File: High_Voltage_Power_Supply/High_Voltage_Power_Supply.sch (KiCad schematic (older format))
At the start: 36 parts

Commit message: Finalised the schematic and BOM
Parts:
- removed C?: 10uF, symbol Device:C
- removed D? (x5): D_ALT, symbol Device:D_ALT
- removed J?: Conn_01x01_Female, symbol Connector:Conn_01x01_Female
- removed R?: 100k, symbol Device:R
- removed R?: 2M, symbol Device:R
- removed R? (x3): 4m, symbol Device:R
- removed R?: 453k, symbol Device:R
- removed R?: inf, symbol Device:R
- added C3: 100uF, Capacitor_THT:CP_Radial_D8.0mm_P5.00mm, symbol Device:CP
- added C6: 10uF, Capacitor_SMD:C_1210_3225Metric, symbol Device:C
- added C8: 1000uF, Capacitor_THT:CP_Radial_D18.0mm_P7.50mm, symbol Device:CP
- added J4: Conn_01x02_Female, Connector_PinHeader_2.54mm:PinHeader_1x02_P2.54mm_Vertical, symbol Connector:Conn_01x02_Female
- added JP1: Jumper_2_Open, Resistor_SMD:R_0603_1608Metric, symbol Jumper:Jumper_2_Open
- added R10: 100k, Resistor_SMD:R_0603_1608Metric, symbol Device:R
- added R12: 453k, Resistor_SMD:R_0805_2012Metric, symbol Device:R
- added R16: 2M, Resistor_SMD:R_1206_3216Metric, symbol Device:R
- added R6, R7, R8: 4m, Resistor_SMD:R_2512_6332Metric, symbol Device:R
- C1: renamed from C?; footprint (none) -> Capacitor_SMD:C_1812_4532Metric; Link (none) -> https://www.digikey.com/product-detail/en/murata-electronic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; Voltage (none) -> >1200V
- C2: renamed from C?; footprint (none) -> Capacitor_SMD:C_0603_1608Metric; Link (none) -> https://www.digikey.com/product-detail/en/murata-electronic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
- C4: renamed from C?; footprint (none) -> Capacitor_SMD:C_1206_3216Metric; Link (none) -> https://www.digikey.com/product-detail/en/murata-electronic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
- C5: renamed from C?; footprint (none) -> Capacitor_SMD:C_1210_3225Metric; Link (none) -> https://www.digikey.com/product-detail/en/murata-electronic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
- C7: renamed from C?; footprint (none) -> Capacitor_THT:CP_Radial_D18.0mm_P7.50mm; Link (none) -> https://www.digikey.com/product-detail/en/nichicon/UPW2A102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
- D1: renamed from D?; value D_ALT -> NDSH25170A; footprint (none) -> Package_TO_SOT_THT:TO-247-2_Vertical; Link (none) -> https://www.digikey.com/product-detail/en/on-semiconductor/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
- J1, J2, J3: renamed from J?; footprint (none) -> Connector:Banana_Jack_2Pin
- Q1: renamed from Q?; footprint (none) -> Package_TO_SOT_THT:TO-264-3_Vertical; symbol Device:Q_NMOS_DGS -> Device:Q_NMOS_SDG; Link (none) -> https://www.digikey.com/product-detail/en/ixys/IXFK180N25T/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
- R1, R2, R3, R9: renamed from R?; footprint (none) -> Resistor_SMD:R_0603_1608Metric; Link (none) -> https://www.digikey.com/product-detail/en/panasonic-electro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
- R11, R13, R14: renamed from R?; footprint (none) -> Resistor_SMD:R_0805_2012Metric; Link (none) -> https://www.digikey.com/product-detail/en/panasonic-electro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; Search https://www.digikey.com/products/en/resistors/chip-resistor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 -> (none)
- R15: renamed from R?; footprint (none) -> Resistor_SMD:R_1206_3216Metric; Link (none) -> https://www.digikey.com/product-detail/en/panasonic-electro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; Search https://www.digikey.com/products/en/resistors/chip-resistor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 -> (none)
- R17: renamed from R?; footprint (none) -> Resistor_SMD:R_1206_3216Metric; Link (none) -> https://www.digikey.com/product-detail/en/panasonic-electro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; search https://www.digikey.com/products/en/resistors/chip-resistor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 -> (none)
- R4: renamed from R?; footprint (none) -> Resistor_SMD:R_0603_1608Metric; 681 Link (none) -> https://www.digikey.com/product-detail/en/panasonic-electro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; 681 search https://www.digikey.com/products/en/resistors/chip-resistor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 -> (none); 787 Link (none) -> https://www.digikey.com/product-detail/en/panasonic-electro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; 787 search https://www.digikey.com/products/en/resistors/chip-resistor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 -> (none)
- R5: renamed from R?; footprint (none) -> Resistor_SMD:R_2512_6332Metric; Link (none) -> https://www.digikey.com/product-detail/en/panasonic-electro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; Search https://www.digikey.com/products/en/resistors/chip-resistor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 -> (none)
- U1: renamed from U?; Link (LT3751E) (none) -> https://www.digikey.com/product-detail/en/analog-devices-in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
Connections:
- wire segments 102 -> 99
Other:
- moved on the sheet: J2

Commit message: Started on the PCB
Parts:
- J1: footprint Connector:Banana_Jack_2Pin -> Connector_PinHeader_2.54mm:PinHeader_1x02_P2.54mm_Vertical
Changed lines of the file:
@@
 F 0 "J1" H 4450 6050 50  0000 C CNN
 F 1 "Conn_01x02_Female" H 4700 5950 50  0000 C CNN
-F 2 "Connector:Banana_Jack_2Pin" H 4450 6250 50  0001 C CNN
+F 2 "Connector_PinHeader_2.54mm:PinHeader_1x02_P2.54mm_Vertical" H 4450 6250 50  0001 C CNN
 F 3 "~" H 4450 6250 50  0001 C CNN
 F 4 "12V" H 4450 6250 50  0001 C CNN "Voltage"
@@
 $EndComp
 $Comp
-L power:GND #PWR?
+L power:GND #PWR0118
 U 1 1 5F322467
 P 2900 3000
-F 0 "#PWR?" H 2900 2750 50  0001 C CNN
+F 0 "#PWR0118" H 2900 2750 50  0001 C CNN
 F 1 "GND" H 2905 2827 50  0000 C CNN
 F 2 "" H 2900 3000 50  0001 C CNN

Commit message: Finished most of the PCB layout
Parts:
- Q1: value Q_NMOS_DGS -> Q_NMOS_GDS; symbol Device:Q_NMOS_SDG -> Device:Q_NMOS_GDS
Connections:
- net at R5.1, R6.1, R7.1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: now also Q1.3 (S); no longer Q1.1 (S)
- net at U1.15 (HVGATE): now also Q1.1 (G); no longer Q1.3 (G)
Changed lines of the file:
@@
 $EndComp
 $Comp
-L Device:Q_NMOS_SDG Q1
+L Device:Q_NMOS_GDS Q1
 U 1 1 5B8B01E1
 P 5400 3400
 F 0 "Q1" H 5605 3446 50  0000 L CNN
-F 1 "Q_NMOS_DGS" H 5605 3355 50  0000 L CNN
+F 1 "Q_NMOS_GDS" H 5605 3355 50  0000 L CNN
 F 2 "Package_TO_SOT_THT:TO-264-3_Vertical" H 5600 3500 50  0001 C CNN
 F 3 "http://ixapps.ixys.com/DataSheet/DS100129A(IXFK-FX180N25T).pdf" H 5400 3400 50  0001 C CNN

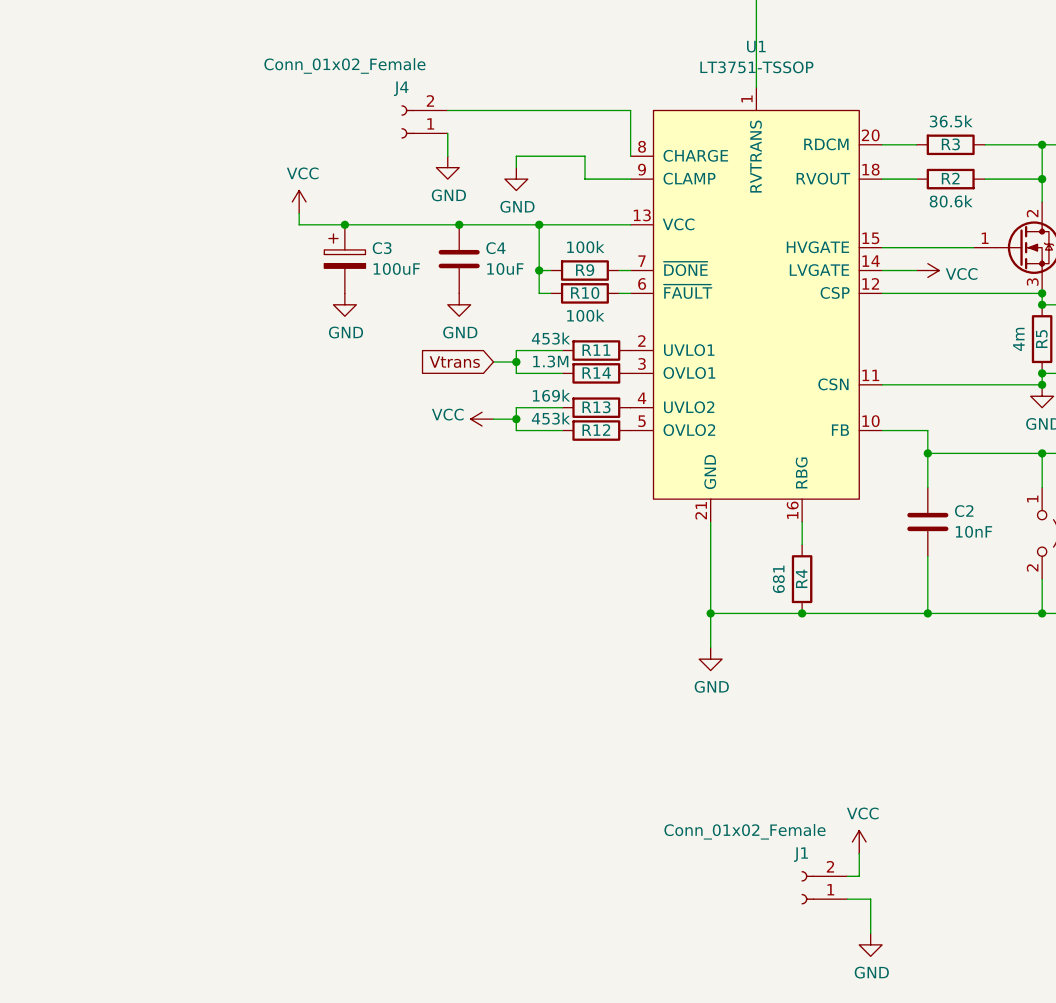
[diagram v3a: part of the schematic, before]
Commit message: Added Done and Fault outputs
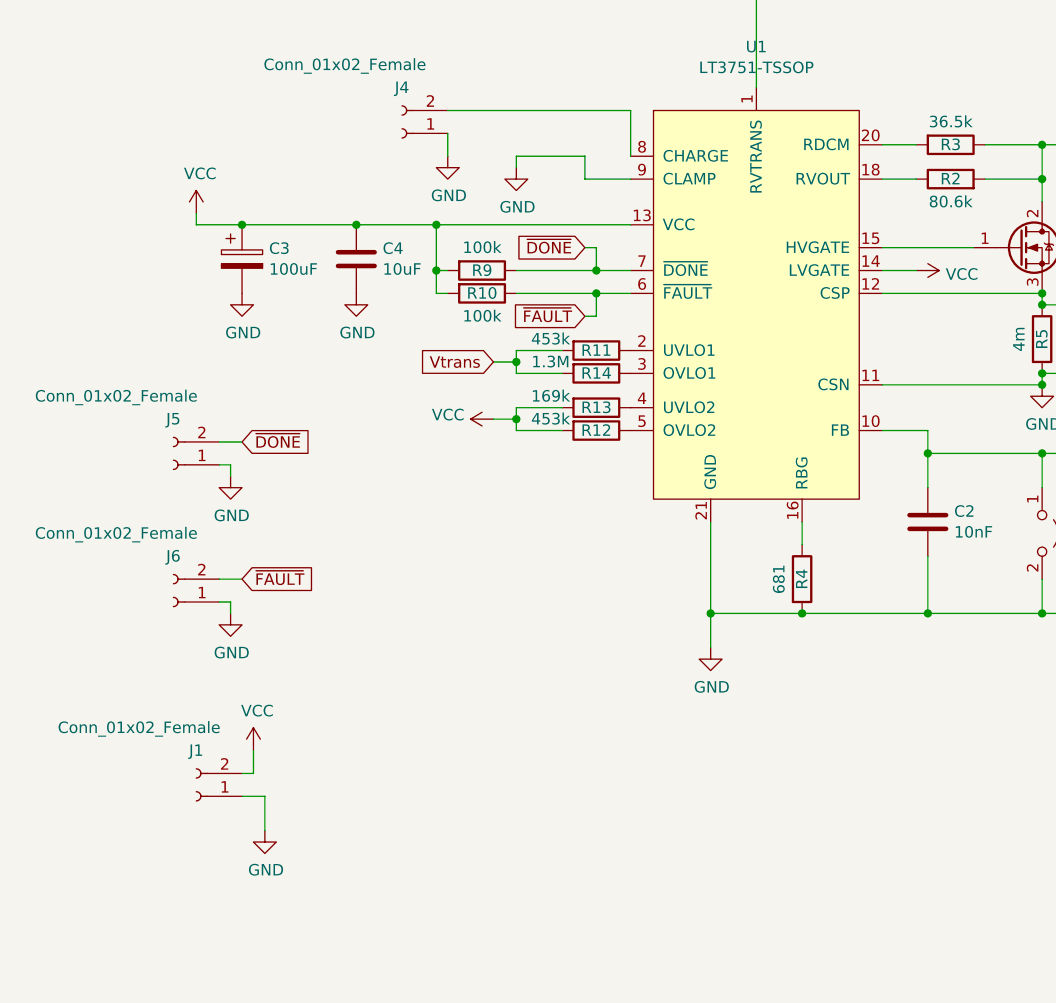
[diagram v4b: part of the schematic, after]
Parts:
- added J5, J6: Conn_01x02_Female, Connector_PinHeader_2.54mm:PinHeader_1x02_P2.54mm_Vertical, symbol Connector:Conn_01x02_Female
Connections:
- net GND: now also J5.1 (Pin_1), J6.1 (Pin_1)
- net ~FAULT~: now reaches R10.1, U1.6 (~FAULT~)
- net ~FAULT~: now also J6.2 (Pin_2)
- net ~DONE~: now reaches R9.1, U1.7 (~DONE~)
- net ~DONE~: now also J5.2 (Pin_2)
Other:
- moved on the sheet: C3, C4, J1, R10, R9

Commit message: Added some notes for it
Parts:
- J3: Voltage (none) -> 1000V
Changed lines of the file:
@@
 F 2 "Connector:Banana_Jack_2Pin" H 9800 2800 50  0001 C CNN
 F 3 "~" H 9800 2800 50  0001 C CNN
+F 4 "1000V" H 9800 2800 50  0001 C CNN "Voltage"
 	1    9800 2800
 	1    0    0    1

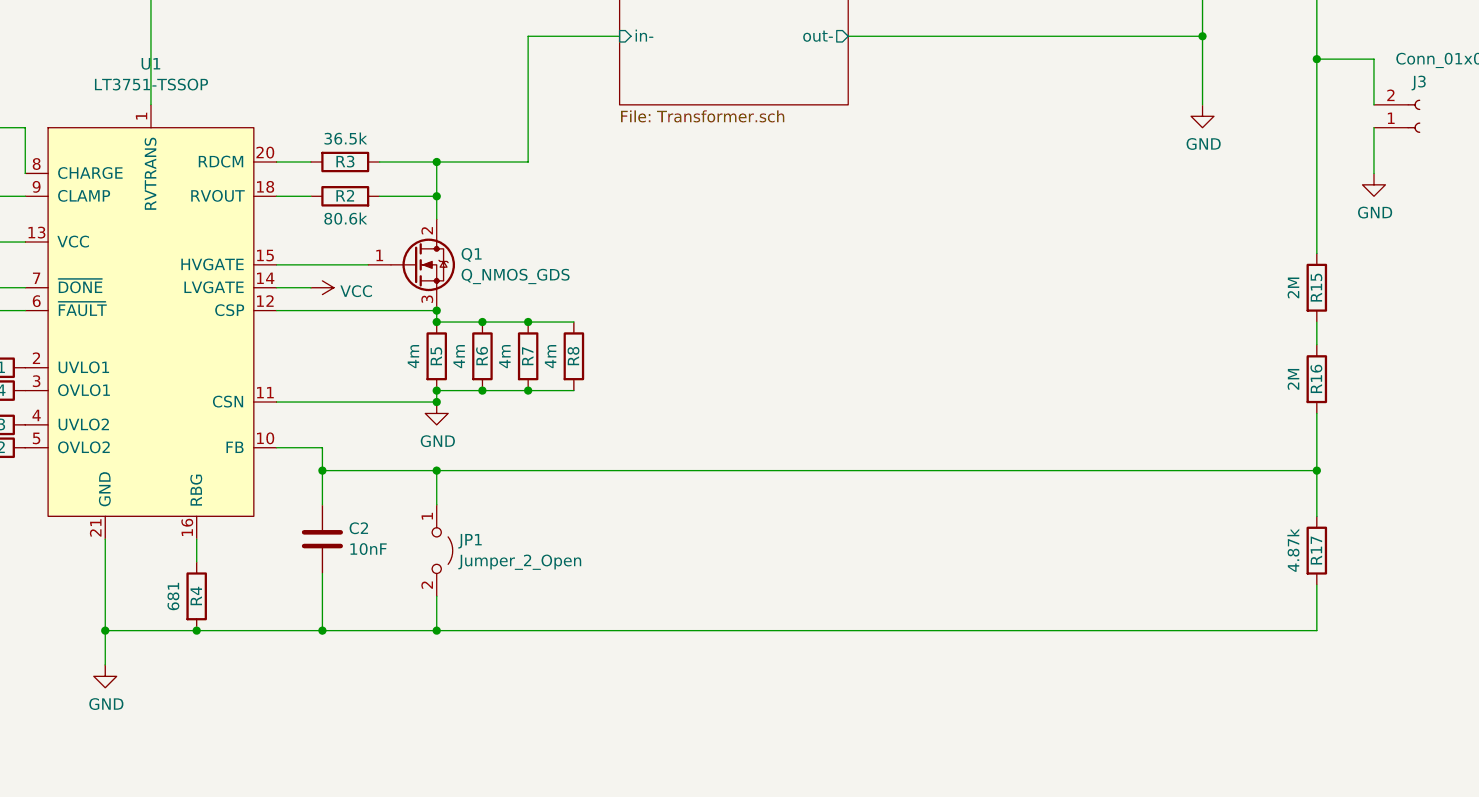
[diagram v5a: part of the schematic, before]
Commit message: Updated schematic to run on regulation mode only
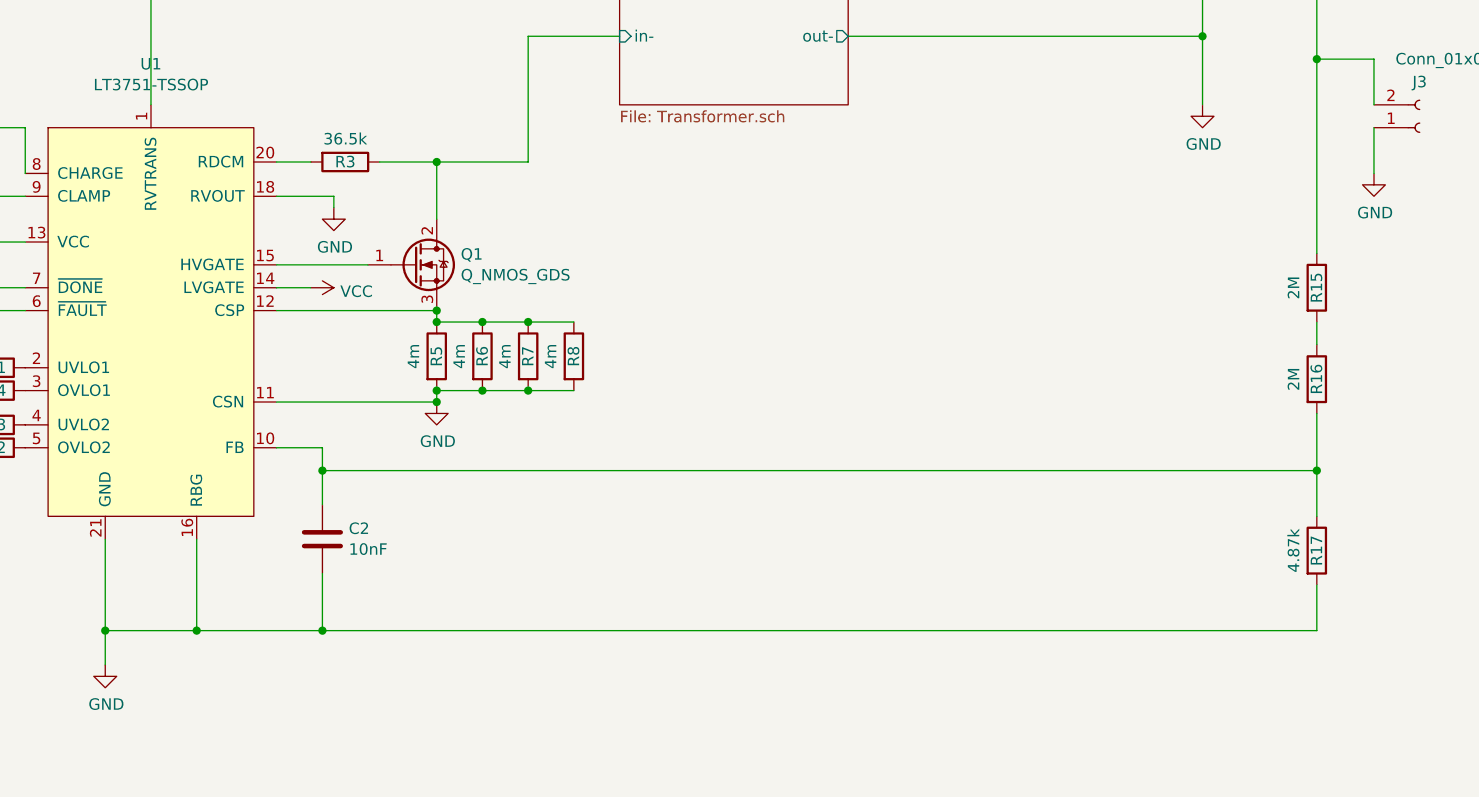
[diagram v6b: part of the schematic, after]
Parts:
- removed JP1: Jumper_2_Open, Resistor_SMD:R_0603_1608Metric, symbol Jumper:Jumper_2_Open
- removed R2: 80.6k, Resistor_SMD:R_0603_1608Metric, symbol Device:R
- removed R4: 681, Resistor_SMD:R_0603_1608Metric, symbol Device:R
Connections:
- net GND: now also U1.16 (RBG), U1.18 (RVOUT)
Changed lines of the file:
@@
 	0    1    1    0
 $EndComp
-$Comp
-L Device:R R2
-U 1 1 5B8A6A21
-P 5100 3100
-F 0 "R2" V 5100 3100 50  0000 C CNN
-F 1 "80.6k" V 5000 3100 50  0000 C CNN
-F 2 "Resistor_SMD:R_0603_1608Metric" V 5030 3100 50  0001 C CNN
-F 3 "https://industrial.panasonic.com/cdbs/www-data/pdf/RDM0000/AOA0000C307.pdf" H 5100 3100 50  0001 C CNN
-F 4 "https://www.digikey.com/product-detail/en/panasonic-electronic-components/ERA-3AEB8062V/P80-6KDBCT-ND/3076062" V 5100 3100 50  0001 C CNN "Link"
-	1    5100 3100
-	0    -1   -1   0
-$EndComp
 Wire Wire Line
 	4800 2950 4950 2950
-Wire Wire Line
-	4800 3100 4950 3100
 $Comp
 L Device:C C4
@@
 	3200 3900 3200 3950
 $Comp
-L Device:R R4
-U 1 1 5B8C18DC
-P 4450 4850
-F 0 "R4" V 4450 4850 50  0000 C CNN
-F 1 "681" V 4350 4850 50  0000 C CNN
-F 2 "Resistor_SMD:R_0603_1608Metric" V 4380 4850 50  0001 C CNN
-F 3 "https://industrial.panasonic.com/cdbs/www-data/pdf/RDM0000/AOA0000C307.pdf" H 4450 4850 50  0001 C CNN
-F 4 "use 681 if using Vout comparitor as backup protection while in regulation mode, 787 if using Vout comparitor directly as trip in chage mode " V 4450 4850 50  0001 C CNN "Note"
-F 5 "https://www.digikey.com/product-detail/en/panasonic-electronic-components/ERA-3AEB6810V/P681DBCT-ND/3076036" V 4450 4850 50  0001 C CNN "681 Link"
-F 6 "https://www.digikey.com/product-detail/en/panasonic-electronic-components/ERA-3AEB7870V/P787DBCT-ND/3076056" V 4450 4850 50  0001 C CNN "787 Link"
-	1    4450 4850
-	1    0    0    -1
-$EndComp
-$Comp
 L power:GND #PWR0110
 U 1 1 5B8C1AD0
@@
 	4050 4600 4050 5000
 Wire Wire Line
-	4050 5000 4450 5000
-Wire Wire Line
 	4050 5000 4050 5150
 Connection ~ 4050 5000
-Wire Wire Line
-	4450 4700 4450 4600
 $Comp
 L Device:C C2
@@
 	1    0    0    -1
 $EndComp
-Connection ~ 4450 5000
 Wire Wire Line
 	5000 4750 5000 5000
@@
 Wire Wire Line
 	5250 2950 5500 2950
-Wire Wire Line
-	5500 2950 5500 3100
-Wire Wire Line
-	5250 3100 5500 3100
-Connection ~ 5500 3100
-Wire Wire Line
-	5500 3100 5500 3200
 Wire Wire Line
 	5900 2950 5500 2950
@@
 Wire Wire Line
 	8850 2700 8850 2400
-Wire Wire Line
-	5000 4300 5500 4300
 Connection ~ 5000 4300
 Wire Wire Line
@@
 	9350 4300 9350 4500
 Wire Wire Line
-	4450 5000 5000 5000
-Wire Wire Line
 	9350 4800 9350 5000
 Connection ~ 5000 5000
-Wire Wire Line
-	5000 5000 5500 5000
 Wire Wire Line
 	4250 2700 4250 2000
@@
 Wire Wire Line
 	3200 3000 3200 3050
-Connection ~ 5500 4300
-Wire Wire Line
-	5500 4300 9350 4300
-Connection ~ 5500 5000
-Wire Wire Line
-	5500 5000 9350 5000
 Text GLabel 6000 1400 2    50   Input ~ 0
 Vtrans
@@
 Wire Wire Line
 	8200 1700 8850 1700
-$Comp
-L Jumper:Jumper_2_Open JP1
-U 1 1 5F2F41C4
-P 5500 4650
-F 0 "JP1" V 5454 4748 50  0000 L CNN
-F 1 "Jumper_2_Open" V 5545 4748 50  0000 L CNN
-F 2 "Resistor_SMD:R_0603_1608Metric" H 5500 4650 50  0001 C CNN
-F 3 "http://industrial.panasonic.com/www-cgi/jvcr13pz.cgi?E+PZ+3+AOA0001+ERJ3GEY0R00V+7+WW" H 5500 4650 50  0001 C CNN
-F 4 "Short this jumper to run device in constant capacitor charging mode" V 5500 4650 50  0001 C CNN "Note"
-F 5 "https://www.digikey.com/product-detail/en/panasonic-electronic-components/ERJ-3GEY0R00V/P0-0GCT-ND/134711" V 5500 4650 50  0001 C CNN "Link"
-	1    5500 4650
-	0    1    1    0
-$EndComp
-Wire Wire Line
-	5500 4450 5500 4300
-Wire Wire Line
-	5500 4850 5500 5000
 Wire Wire Line
 	5500 3650 5700 3650
@@
 Wire Wire Line
 	1950 4950 1950 5000
+Wire Wire Line
+	5000 4300 9350 4300
+Wire Wire Line
+	5000 5000 9350 5000
+Wire Wire Line
+	4050 5000 4450 5000
+Wire Wire Line
+	4450 4600 4450 5000
+Connection ~ 4450 5000
+Wire Wire Line
+	4450 5000 5000 5000
+Wire Wire Line
+	5500 2950 5500 3200
+$Comp
+L power:GND #PWR?
+U 1 1 5F796AD5
+P 5050 3150
+F 0 "#PWR?" H 5050 2900 50  0001 C CNN
+F 1 "GND" H 5055 2977 50  0000 C CNN
+F 2 "" H 5050 3150 50  0001 C CNN
+F 3 "" H 5050 3150 50  0001 C CNN
+	1    5050 3150
+	1    0    0    -1
+$EndComp
+Wire Wire Line
+	5050 3100 5050 3150
+Wire Wire Line
+	4800 3100 5050 3100
 $EndSCHEMATC

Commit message: Started design of the ignitor circuit
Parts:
- removed J5: Conn_01x02_Female, Connector_PinHeader_2.54mm:PinHeader_1x02_P2.54mm_Vertical, symbol Connector:Conn_01x02_Female
- added C? (x2): 10uF, Capacitor_SMD:C_1210_3225Metric, symbol Device:C
- added C? (x2): 1000uF, Capacitor_THT:CP_Radial_D18.0mm_P7.50mm, symbol Device:CP
- added C?: 10uF, Capacitor_SMD:C_1206_3216Metric, symbol Device:C
- added C?: 10nF, Capacitor_SMD:C_0603_1608Metric, symbol Device:C
- added C?: 2200pF, Capacitor_SMD:C_1812_4532Metric, symbol Device:C
- added C?: 100uF, Capacitor_THT:CP_Radial_D8.0mm_P5.00mm, symbol Device:CP
- added D?: NDSH25170A, Package_TO_SOT_THT:TO-247-2_Vertical, symbol Device:D_ALT
- added J?: Conn_01x02_Female, Connector:Banana_Jack_2Pin, symbol Connector:Conn_01x02_Female
- added J? (x2): Conn_01x02_Female, Connector_PinHeader_2.54mm:PinHeader_1x02_P2.54mm_Vertical, symbol Connector:Conn_01x02_Female
- added Q?: Q_NMOS_GDS, Package_TO_SOT_THT:TO-264-3_Vertical, symbol Device:Q_NMOS_GDS
- added R?: 4.87k, Resistor_SMD:R_1206_3216Metric, symbol Device:R
- added R? (x2): 2M, Resistor_SMD:R_1206_3216Metric, symbol Device:R
- added R?: 80.6k, Resistor_SMD:R_0603_1608Metric, symbol Device:R
- added R?: 36.5k, Resistor_SMD:R_0603_1608Metric, symbol Device:R
- added R? (x2): 100k, Resistor_SMD:R_0603_1608Metric, symbol Device:R
- added R? (x2): 4m, Resistor_SMD:R_2512_6332Metric, symbol Device:R
- added R? (x2): 453k, Resistor_SMD:R_0805_2012Metric, symbol Device:R
- added R?: 169k, Resistor_SMD:R_0805_2012Metric, symbol Device:R
- added R?: 1.3M, Resistor_SMD:R_0805_2012Metric, symbol Device:R
- added TR?: GA3460-BL, High_Voltage_Power_Supply:Transformer_Coilcraft_GA3460-BL, symbol High_Voltage_Power_Supply:GA3460-BL
- added U?: LT3751-TSSOP, Package_SO:HTSSOP-20-1EP_4.4x6.5mm_P0.65mm_EP3.4x6.5mm_ThermalVias, symbol High_Voltage_Power_Supply:LT3751-TSSOP
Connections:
- net GND: now also C?.2, C?.2, C?.2, C?.2, C?.2, C?.2, C?.2, C?.2, J?.1 (Pin_1), J?.1 (Pin_1), J?.1 (Pin_1), R?.2, R?.2, R?.2, TR?.7, U?.11 (CSN), U?.16 (RBG), U?.18 (RVOUT), U?.21 (GND), U?.9 (CLAMP)
- net VCC: now also C?.1, C?.1, R?.2, R?.2, R?.2, R?.2, U?.13 (VCC), U?.14 (LVGATE)
- net Vtrans: now also C?.1, C?.1, C?.1, C?.1, R?.1, R?.2, R?.2, TR?.1, TR?.2, TR?.3, TR?.4
- net ~DONE~: no longer names the net of R9.1, U1.7 (~DONE~)
- new net: C?.1, R?.1, R?.2, U?.10 (FB)
- new net: C?.1, D?.1 (K), J?.2 (Pin_2), R?.1
- new net: R?.1, R?.2
- new net: R?.2, U?.1 (RVTRANS)
- new net: Q?.3 (S), R?.1, R?.1, U?.12 (CSP)
- new net: Q?.1 (G), U?.15 (HVGATE)
- new net: R?.1, U?.2 (UVLO1)
- new net: R?.2, U?.20 (RDCM)
- new net: R?.1, U?.3 (OVLO1)
- new net: R?.1, U?.4 (UVLO2)
- new net: R?.1, U?.5 (OVLO2)
- new net: R?.1, U?.7 (~DONE~)
- new net: J?.2 (Pin_2), U?.8 (CHARGE)
- new net: Q?.2 (D), R?.1, TR?.10, TR?.11, TR?.12, TR?.9
- new net: D?.2 (A), TR?.6
- new net ~FAULT_IGN~: J?.2 (Pin_2), R?.1, U?.6 (~FAULT~)
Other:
- moved on the sheet: C1, C2, C3, C4, C5, C6, C7, C8, D1, J1, J2, J3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
